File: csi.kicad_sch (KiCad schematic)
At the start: 39 parts, among them J11 F32R-1A7H1-11022, J13 F32R-1A7H1-11022, U11 SN74LV1T125DCKR, U3 SN74LV1T125DCKR, U9 TS3USB30ERSWR

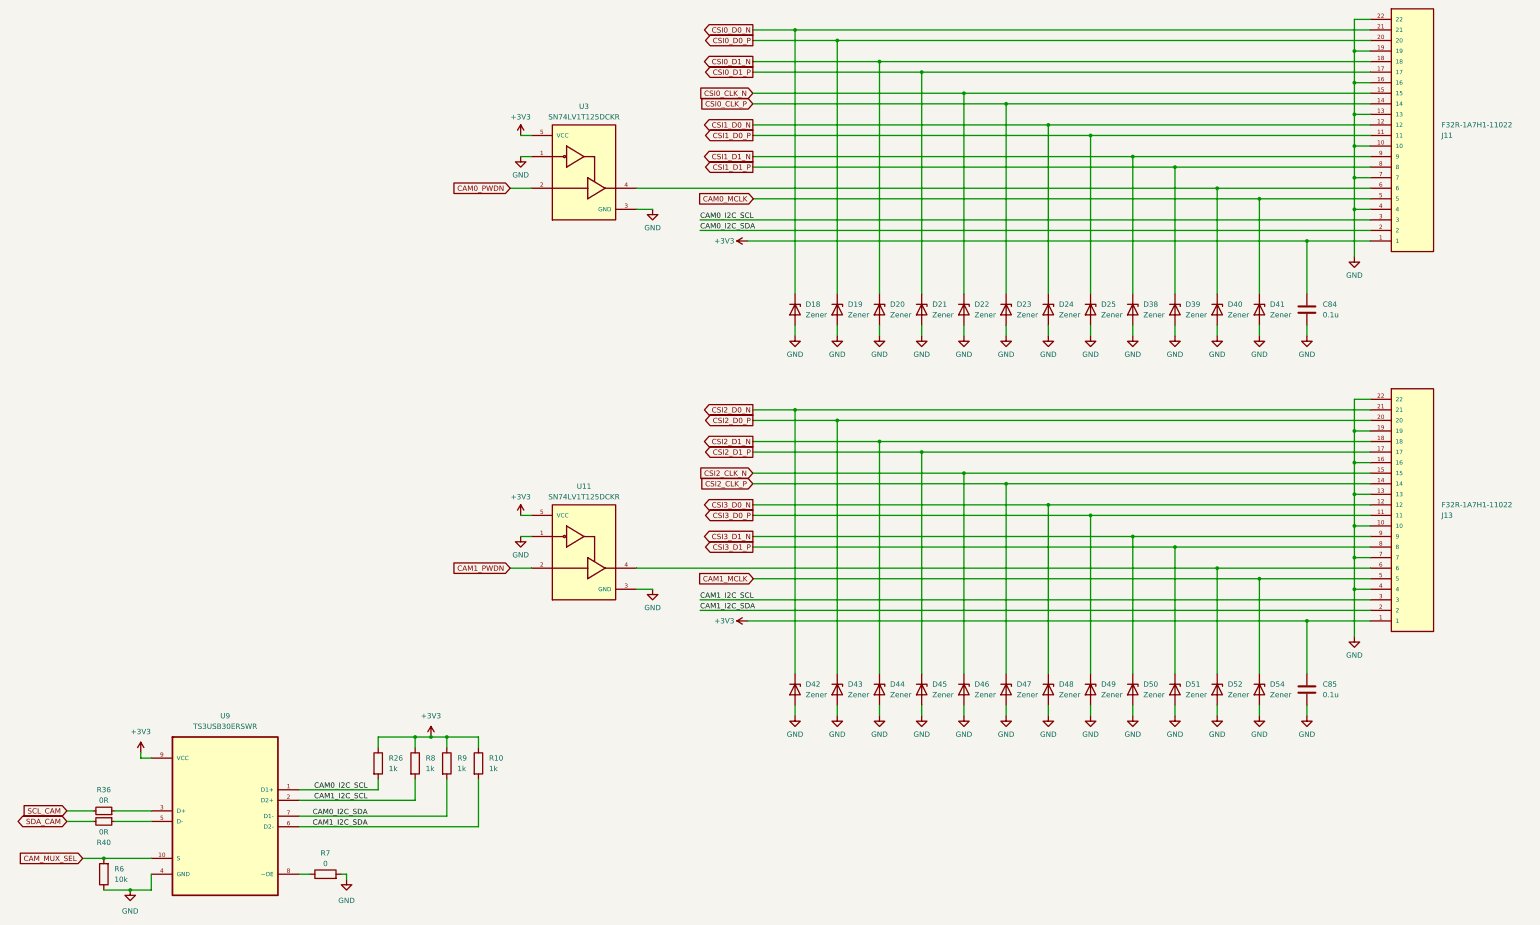
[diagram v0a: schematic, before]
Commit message: Schematic V1 and footprints assigned
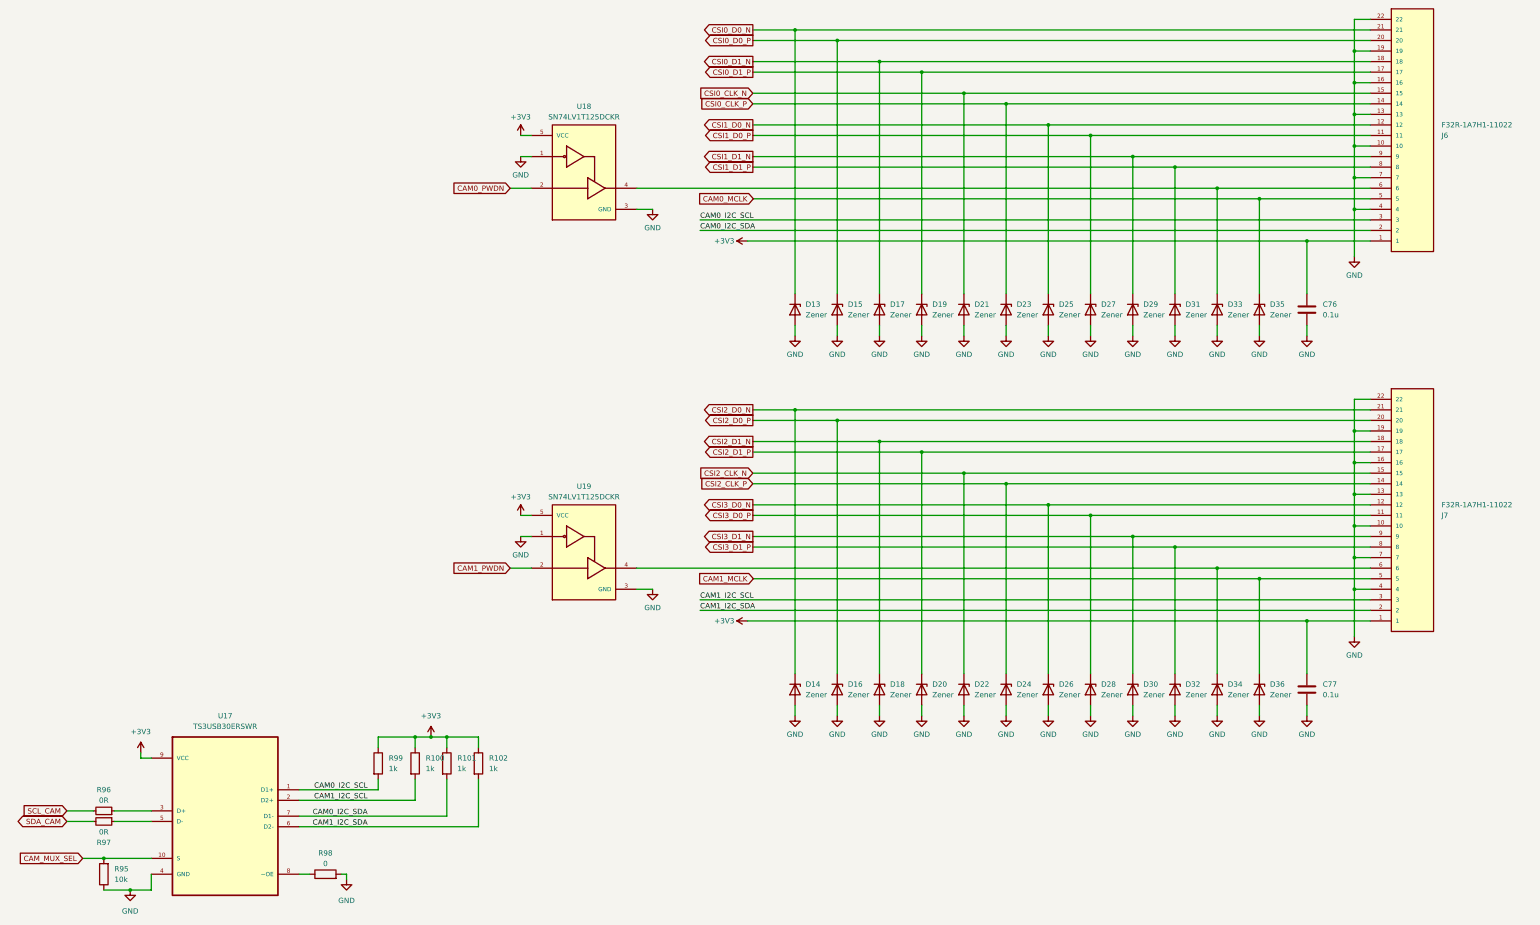
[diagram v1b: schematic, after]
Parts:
- C76: renamed from C84; footprint (none) -> jetson-orin-baseboard-footprints:0402-cap
- C77: renamed from C85; footprint (none) -> jetson-orin-baseboard-footprints:0402-cap
- D13: renamed from D18; footprint (none) -> jetson-orin-baseboard-footprints:DFN1006-2
- D14: renamed from D42; footprint (none) -> jetson-orin-baseboard-footprints:DFN1006-2
- D15: renamed from D19; footprint (none) -> jetson-orin-baseboard-footprints:DFN1006-2
- D16: renamed from D43; footprint (none) -> jetson-orin-baseboard-footprints:DFN1006-2
- D17: renamed from D20; footprint (none) -> jetson-orin-baseboard-footprints:DFN1006-2
- D18: renamed from D44; footprint (none) -> jetson-orin-baseboard-footprints:DFN1006-2
- D19: renamed from D21; footprint (none) -> jetson-orin-baseboard-footprints:DFN1006-2
- D20: renamed from D45; footprint (none) -> jetson-orin-baseboard-footprints:DFN1006-2
- D21: renamed from D22; footprint (none) -> jetson-orin-baseboard-footprints:DFN1006-2
- D22: renamed from D46; footprint (none) -> jetson-orin-baseboard-footprints:DFN1006-2
- D23: footprint (none) -> jetson-orin-baseboard-footprints:DFN1006-2
- D24: renamed from D47; footprint (none) -> jetson-orin-baseboard-footprints:DFN1006-2
- D25: renamed from D24; footprint (none) -> jetson-orin-baseboard-footprints:DFN1006-2
- D26: renamed from D48; footprint (none) -> jetson-orin-baseboard-footprints:DFN1006-2
- D27: renamed from D25; footprint (none) -> jetson-orin-baseboard-footprints:DFN1006-2
- D28: renamed from D49; footprint (none) -> jetson-orin-baseboard-footprints:DFN1006-2
- D29: renamed from D38; footprint (none) -> jetson-orin-baseboard-footprints:DFN1006-2
- D30: renamed from D50; footprint (none) -> jetson-orin-baseboard-footprints:DFN1006-2
- D31: renamed from D39; footprint (none) -> jetson-orin-baseboard-footprints:DFN1006-2
- D32: renamed from D51; footprint (none) -> jetson-orin-baseboard-footprints:DFN1006-2
- D33: renamed from D40; footprint (none) -> jetson-orin-baseboard-footprints:DFN1006-2
- D34: renamed from D52; footprint (none) -> jetson-orin-baseboard-footprints:DFN1006-2
- D35: renamed from D41; footprint (none) -> jetson-orin-baseboard-footprints:DFN1006-2
- D36: renamed from D54; footprint (none) -> jetson-orin-baseboard-footprints:DFN1006-2
- J6: renamed from J11; footprint F32R-1A7H1-11022:AMPHENOL_F32R-1A7H1-11022 -> jetson-orin-baseboard-footprints:AMPHENOL_F32R-1A7H1-11022
- J7: renamed from J13; footprint F32R-1A7H1-11022:AMPHENOL_F32R-1A7H1-11022 -> jetson-orin-baseboard-footprints:AMPHENOL_F32R-1A7H1-11022
- R100: renamed from R8; footprint (none) -> jetson-orin-baseboard-footprints:0402-res
- R101: renamed from R9; footprint (none) -> jetson-orin-baseboard-footprints:0402-res
- R102: renamed from R10; footprint (none) -> jetson-orin-baseboard-footprints:0402-res
- R95: renamed from R6; footprint (none) -> jetson-orin-baseboard-footprints:0402-res
- R96: renamed from R36; footprint jetson-orin-baseboard-footprints:R_0402_1005Metric -> jetson-orin-baseboard-footprints:0402-res
- R97: renamed from R40; footprint jetson-orin-baseboard-footprints:R_0402_1005Metric -> jetson-orin-baseboard-footprints:0402-res
- R98: renamed from R7; footprint (none) -> jetson-orin-baseboard-footprints:0402-res
- R99: renamed from R26; footprint (none) -> jetson-orin-baseboard-footprints:0402-res
- U17: renamed from U9; footprint TS3USB30ERSWR:QFN40P140X180X55-10N -> jetson-orin-baseboard-footprints:QFN40P140X180X55-10N
- U18: renamed from U3; footprint SN74LV1T125DCKR:SOT65P210X110-5N -> jetson-orin-baseboard-footprints:SOT65P210X110-5N
- U19: renamed from U11; footprint SN74LV1T125DCKR:SOT65P210X110-5N -> jetson-orin-baseboard-footprints:SOT65P210X110-5N

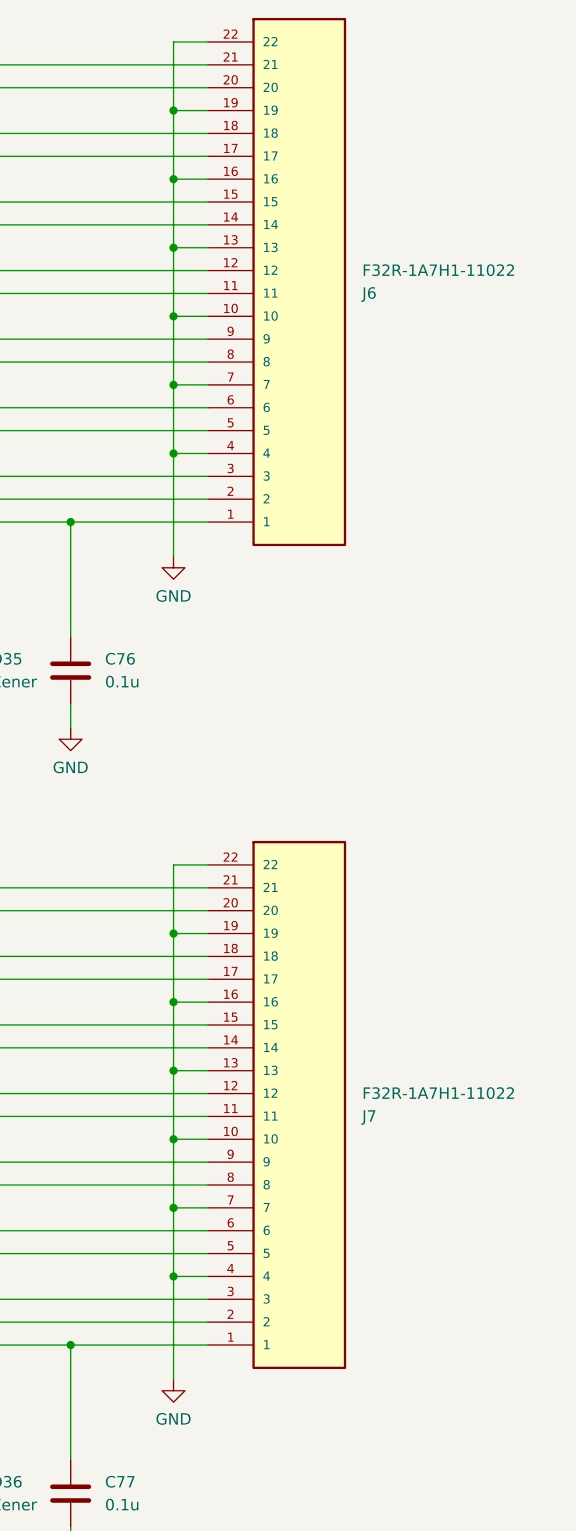
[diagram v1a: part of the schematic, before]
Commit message: Footprints well assigned, XT30 added, Shields grounded
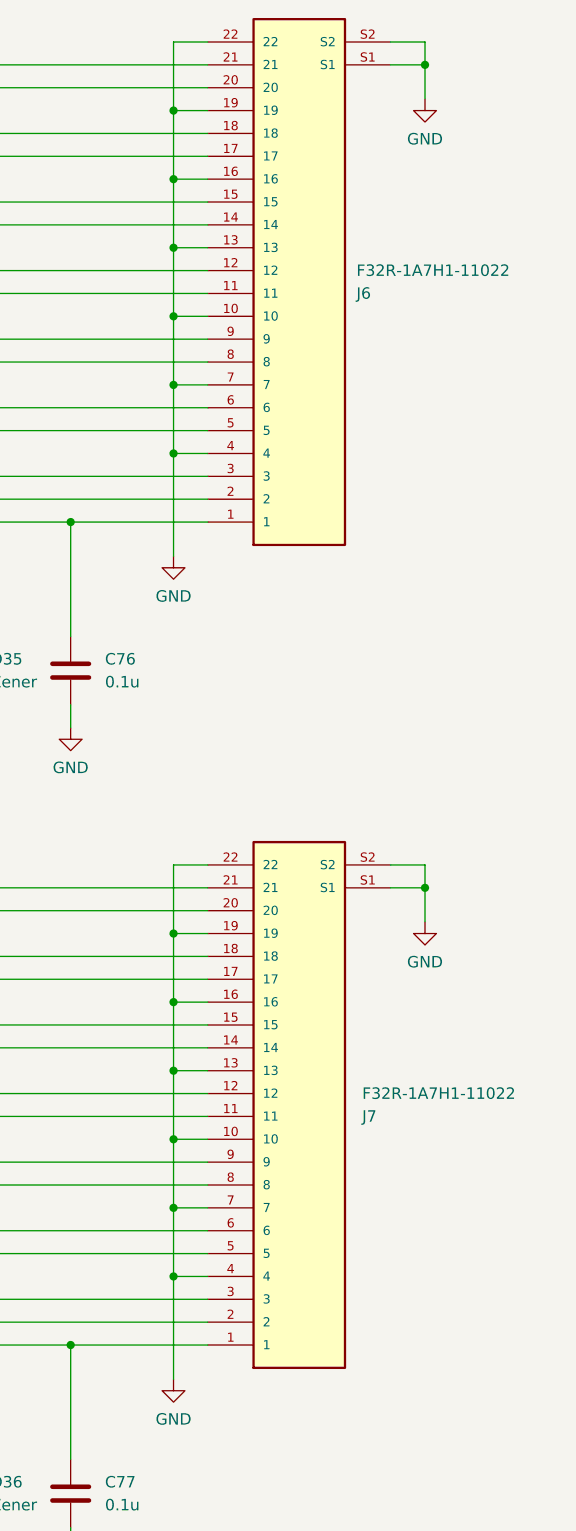
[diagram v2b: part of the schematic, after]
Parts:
- removed D13, D14, D15, D16, D17, D18, D19, D20, D21, D22, D23, D24, D25, D26, D27, D28, D29, D30, D31, D32, D33, D34, D35, D36: Zener, jetson-orin-baseboard-footprints:DFN1006-2, symbol Device:D_Zener
- added D13, D14, D15, D16, D17, D18, D19, D20, D21, D22, D23, D24, D25, D26, D27, D28, D29, D30, D31, D32, D33, D34, D35, D36: Zener, jetson-orin-baseboard-footprints:DFN1006-2, symbol jetson-orin-baseboard:D_Zener
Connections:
- net CAM0_MCLK: now also D35.K
- net CAM1_MCLK: now also D36.K
- net CSI0_CLK_N: now also D21.K
- net CSI0_CLK_P: now also D23.K
- net CSI0_D0_N: now also D13.K
- net CSI0_D0_P: now also D15.K
- net CSI0_D1_N: now also D17.K
- net CSI0_D1_P: now also D19.K
- net CSI1_D0_N: now also D25.K
- net CSI1_D0_P: now also D27.K
- net CSI1_D1_N: now also D29.K
- net CSI1_D1_P: now also D31.K
- net CSI2_CLK_N: now also D22.K
- net CSI2_CLK_P: now also D24.K
- net CSI2_D0_N: now also D14.K
- net CSI2_D0_P: now also D16.K
- net CSI2_D1_N: now also D18.K
- net CSI2_D1_P: now also D20.K
- net CSI3_D0_N: now also D26.K
- net CSI3_D0_P: now also D28.K
- net CSI3_D1_N: now also D30.K
- net CSI3_D1_P: now also D32.K
- net GND: now also J6.S1, J6.S2, J7.S1, J7.S2, D13.A, D14.A, D15.A, D16.A, D17.A, D18.A, D19.A, D20.A, D21.A, D22.A, D23.A, D24.A, D25.A, D26.A, D27.A, D28.A, D29.A, D30.A, D31.A, D32.A, D33.A, D34.A, D35.A, D36.A
- net at J6.6, U18.4: now also D33.K
- net at J7.6, U19.4: now also D34.K

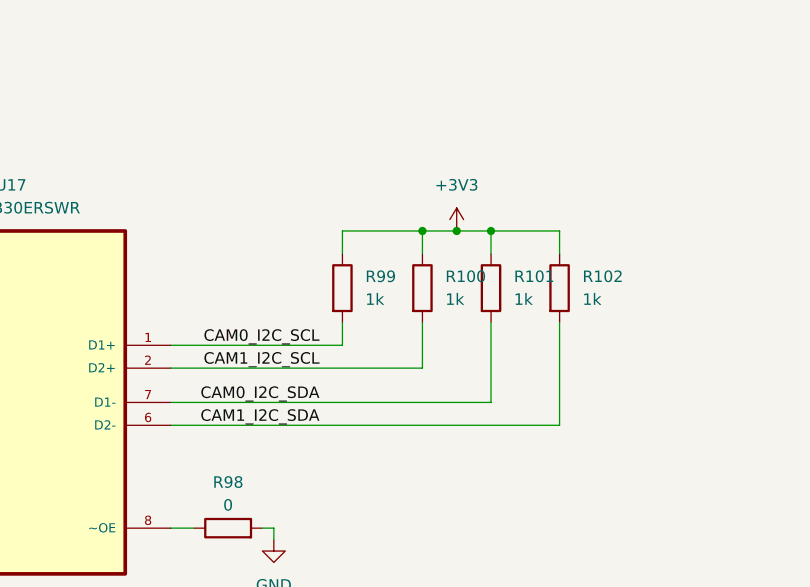
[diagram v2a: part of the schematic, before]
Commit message: Text size changes and positioning important components part 1
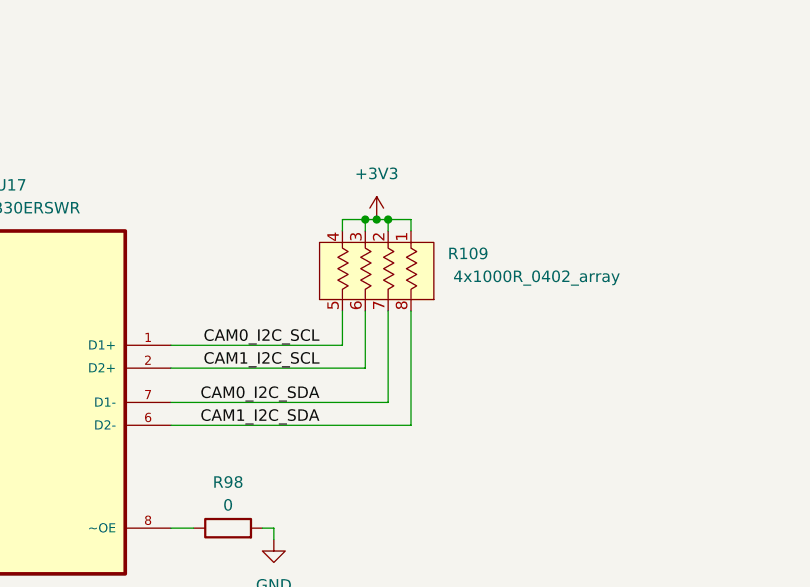
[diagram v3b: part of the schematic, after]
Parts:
- removed R100, R101, R102, R99: 1k, jetson-orin-baseboard-footprints:0402-res, symbol Device:R
- added R109: 4x1000R_0402_array, jetson-orin-baseboard-footprints:R_Array_4x0402, symbol jetson-orin-baseboard:4x330R_0402_array
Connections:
- net +3V3: now also R109.1, R109.2, R109.3, R109.4
- net CAM0_I2C_SCL: now also R109.5
- net CAM0_I2C_SDA: now also R109.7
- net CAM1_I2C_SCL: now also R109.6
- net CAM1_I2C_SDA: now also R109.8
